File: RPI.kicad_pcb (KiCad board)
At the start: 2 copper layers, 65 x 56 mm, 31 parts, among them J1 Conn_01x02_Male, J2 GPIO, J5 Conn_01x06, J6 Conn_01x04, J7 Conn_01x03, J8 Conn_01x02, J9 Conn_01x02, Q1 IRF9540N, Q2 IRF9540N, Q3 BC856BDW1, SW1 SW_SPDT, SW2 SW_SPDT, U1 LM1085-ADJ

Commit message: Official completion (Maybe add Gerald in)
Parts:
- added G***: LOGO, LOGO, F.Cu at (124.0, 96.2)
- added ROBOTS101: LOGO, LOGO, F.Cu at (115.4, 59.9)
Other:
- board text added: "Motor LED"
- board text added: "Power Jumper"
- board text added: "Rasp Pi LED"
- board text added: "Remove jumper if powering board from the Raspberry Pi Keep jumper if powering board from the battery"
- board text removed: "R-Pi Batt Power Jumper"

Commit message: Student Version
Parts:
- removed C1: 10u, Capacitor_THT:CP_Radial_D5.0mm_P2.50mm
- removed C2: 10nF, Capacitor_SMD:C_0805_2012Metric_Pad1.18x1.45mm_HandSolder
- removed C3: 10uF, Capacitor_SMD:C_0805_2012Metric_Pad1.18x1.45mm_HandSolder
- removed C_Tan1: 10u, Capacitor_Tantalum_SMD:CP_EIA-2012-12_Kemet-R_Pad1.30x1.05mm_HandSolder
- removed D1, D2: LED, Diode_SMD:D_0805_2012Metric_Pad1.15x1.40mm_HandSolder
- removed D3, D4: 1N52318, Diode_THT:D_DO-35_SOD27_P7.62mm_Horizontal
- removed G***, ROBOTS101: LOGO, LOGO
- removed Q1, Q2: IRF9540N, Package_TO_SOT_THT:TO-220-3_Vertical
- removed Q3: BC856BDW1, Package_TO_SOT_SMD:SOT-363_SC-70-6
- removed R1: 121, Resistor_SMD:R_0805_2012Metric_Pad1.20x1.40mm_HandSolder
- removed R2: 365, Resistor_SMD:R_0805_2012Metric_Pad1.20x1.40mm_HandSolder
- removed R3, R4: R, Resistor_SMD:R_0805_2012Metric_Pad1.20x1.40mm_HandSolder
- removed R5: 10k, Resistor_SMD:R_0805_2012Metric_Pad1.20x1.40mm_HandSolder
- removed R6: 47k, Resistor_SMD:R_0805_2012Metric_Pad1.20x1.40mm_HandSolder
- removed SW1, SW2: SW_SPDT, RPi_Hat:Switch_SPDT_Jaycar
- removed U1: LM1085-ADJ, RPi_Hat:LM1085-5.0
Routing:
- net VCC: track 105.4 -> 0.00 mm
- net +5V: track 83.8 -> 0.00 mm, vias 1 -> 0
- net /GPIO2/SDA1: track 64.5 -> 0.53 mm
- net /GPIO3/SCL1: track 60.1 -> 0.68 mm
- net /GPIO4/GPCLK: track 52.9 -> 0.00 mm
- net VDDA: track 52.8 -> 0.00 mm
- net Net-(Q1-Pad3): track 48.4 -> 0.00 mm
- net +BATT: track 46.7 -> 0.00 mm
- net VD: track 42.2 -> 0.00 mm, vias 1 -> 0
- net /GPIO9/MISO: track 33.3 -> 0.00 mm
- net Net-(Q2-Pad1): track 32.7 -> 0.00 mm
- net /GPIO27/GEN2: track 32.0 -> 0.00 mm
- net /GPIO17/GEN0: track 28.4 -> 0.00 mm
- net /GPIO18/GEN1: track 23.0 -> 0.00 mm
- net Net-(R1-Pad2): track 22.7 -> 0.00 mm
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- removed copper zone on B.Cu, net GND
- removed copper zone on F.Cu, net GND
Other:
- board text removed: "3.3V"
- board text removed: "5V"
- board text removed: "Battery Switch"
- board text removed: "Board Protection"
- board text removed: "GND"
- board text removed: "GPIO17"
- board text removed: "GPIO18"
- board text removed: "GPIO2"
- board text removed: "GPIO27"
- board text removed: "GPIO3"
- board text removed: "GPIO4"
- board text removed: "GPIO9"
- board text removed: "Motor Control"
- board text removed: "Motor LED"
- board text removed: "Motor Pow"
- board text removed: "Power Jumper"
- board text removed: "Rasp Pi LED"
- board text removed: "Rasp Pi Protection"
- board text removed: "Rasp Pi Switch"
- board text removed: "Remove jumper if powering board from the Raspberry Pi Keep jumper if powering board from the battery"
- board text removed: "Servo Motor"
- board text removed: "Ultrasonic Sensor"
- board text removed: "V Batt"
- board text removed: "Voltage Reg"

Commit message: Revert "Student Version"
This reverts commit 96f77fa7ec59c85fd2b51f56cc1ae2b80deb0d98.
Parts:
- added C1: 10u, Capacitor_THT:CP_Radial_D5.0mm_P2.50mm, F.Cu at (154.8, 65.5)
- added C2: 10nF, Capacitor_SMD:C_0805_2012Metric_Pad1.18x1.45mm_HandSolder, F.Cu at (111.0, 67.0)
- added C3: 10uF, Capacitor_SMD:C_0805_2012Metric_Pad1.18x1.45mm_HandSolder, F.Cu at (111.0, 73.0)
- added C_Tan1: 10u, Capacitor_Tantalum_SMD:CP_EIA-2012-12_Kemet-R_Pad1.30x1.05mm_HandSolder, B.Cu at (141.9, 62.8)
- added D1: LED, Diode_SMD:D_0805_2012Metric_Pad1.15x1.40mm_HandSolder, F.Cu at (134.0, 73.0)
- added D2: LED, Diode_SMD:D_0805_2012Metric_Pad1.15x1.40mm_HandSolder, F.Cu at (134.0, 67.0)
- added D3: 1N52318, Diode_THT:D_DO-35_SOD27_P7.62mm_Horizontal, F.Cu at (123.8, 73.0)
- added D4: 1N52318, Diode_THT:D_DO-35_SOD27_P7.62mm_Horizontal, F.Cu at (123.8, 67.0)
- added G***: LOGO, LOGO, F.Cu at (124.0, 96.2)
- added Q1: IRF9540N, Package_TO_SOT_THT:TO-220-3_Vertical, F.Cu at (128.0, 89.1)
- added Q2: IRF9540N, Package_TO_SOT_THT:TO-220-3_Vertical, F.Cu at (128.0, 81.0)
- added Q3: BC856BDW1, Package_TO_SOT_SMD:SOT-363_SC-70-6, B.Cu at (142.0, 57.0)
- added R1: 121, Resistor_SMD:R_0805_2012Metric_Pad1.20x1.40mm_HandSolder, B.Cu at (134.0, 56.2)
- added R2: 365, Resistor_SMD:R_0805_2012Metric_Pad1.20x1.40mm_HandSolder, B.Cu at (129.0, 56.2)
- added R3: R, Resistor_SMD:R_0805_2012Metric_Pad1.20x1.40mm_HandSolder, B.Cu at (123.7, 56.2)
- added R4: R, Resistor_SMD:R_0805_2012Metric_Pad1.20x1.40mm_HandSolder, B.Cu at (123.7, 62.0)
- added R5: 10k, Resistor_SMD:R_0805_2012Metric_Pad1.20x1.40mm_HandSolder, B.Cu at (129.0, 62.0)
- added R6: 47k, Resistor_SMD:R_0805_2012Metric_Pad1.20x1.40mm_HandSolder, B.Cu at (134.0, 62.2)
- added ROBOTS101: LOGO, LOGO, F.Cu at (115.4, 59.9)
- added SW1: SW_SPDT, RPi_Hat:Switch_SPDT_Jaycar, F.Cu at (153.5, 77.0)
- added SW2: SW_SPDT, RPi_Hat:Switch_SPDT_Jaycar, F.Cu at (153.5, 89.0)
- added U1: LM1085-ADJ, RPi_Hat:LM1085-5.0, F.Cu at (152.0, 55.0)
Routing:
- net VCC: track 0.00 -> 105.4 mm
- net +5V: track 0.00 -> 83.8 mm, vias 0 -> 1
- net /GPIO2/SDA1: track 0.53 -> 64.5 mm
- net /GPIO3/SCL1: track 0.68 -> 60.1 mm
- net /GPIO4/GPCLK: track 0.00 -> 52.9 mm
- net VDDA: track 0.00 -> 52.8 mm
- net Net-(Q1-Pad3): track 0.00 -> 48.4 mm
- net +BATT: track 0.00 -> 46.7 mm
- net VD: track 0.00 -> 42.2 mm, vias 0 -> 1
- net /GPIO9/MISO: track 0.00 -> 33.3 mm
- net Net-(Q2-Pad1): track 0.00 -> 32.7 mm
- net /GPIO27/GEN2: track 0.00 -> 32.0 mm
- net /GPIO17/GEN0: track 0.00 -> 28.4 mm
- net /GPIO18/GEN1: track 0.00 -> 23.0 mm
- net Net-(R1-Pad2): track 0.00 -> 22.7 mm
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- added copper zone on B.Cu, net GND
- added copper zone on F.Cu, net GND
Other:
- board text added: "3.3V"
- board text added: "5V"
- board text added: "Battery Switch"
- board text added: "Board Protection"
- board text added: "GND"
- board text added: "GPIO17"
- board text added: "GPIO18"
- board text added: "GPIO2"
- board text added: "GPIO27"
- board text added: "GPIO3"
- board text added: "GPIO4"
- board text added: "GPIO9"
- board text added: "Motor Control"
- board text added: "Motor LED"
- board text added: "Motor Pow"
- board text added: "Power Jumper"
- board text added: "Rasp Pi LED"
- board text added: "Rasp Pi Protection"
- board text added: "Rasp Pi Switch"
- board text added: "Remove jumper if powering board from the Raspberry Pi Keep jumper if powering board from the battery"
- board text added: "Servo Motor"
- board text added: "Ultrasonic Sensor"
- board text added: "V Batt"
- board text added: "Voltage Reg"

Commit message: Added Fuse
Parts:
- added F1: MCCQ-122, RPi_Hat:MCCQ122, F.Cu at (124.3, 79.3)
- added G***: LOGO, LOGO, F.Cu at (153.8, 61.6)
- C2: renamed from C_Tan1; value 10u -> 100u
- moved Q1 6.08 mm to (134.1, 89.1)
- moved Q2 6.08 mm to (134.1, 81.0)
- renumbered C2 to C3, C3 to C4
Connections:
- Q1 pad 2: Net-(J1-Pad2) -> Net-(F1-Pad3)
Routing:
- net Net-(F1-Pad3): track 0.00 -> 20.1 mm
- net Net-(Q1-Pad3): track 48.4 -> 41.9 mm
- net VCC: track 105.4 -> 102.8 mm
- net VDDA: track 52.8 -> 50.3 mm
- net VD: track 42.2 -> 39.7 mm
- net Net-(J1-Pad2): track 19.7 -> 17.7 mm
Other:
- board text added: "F1"
- board text added: "Main Fuse"

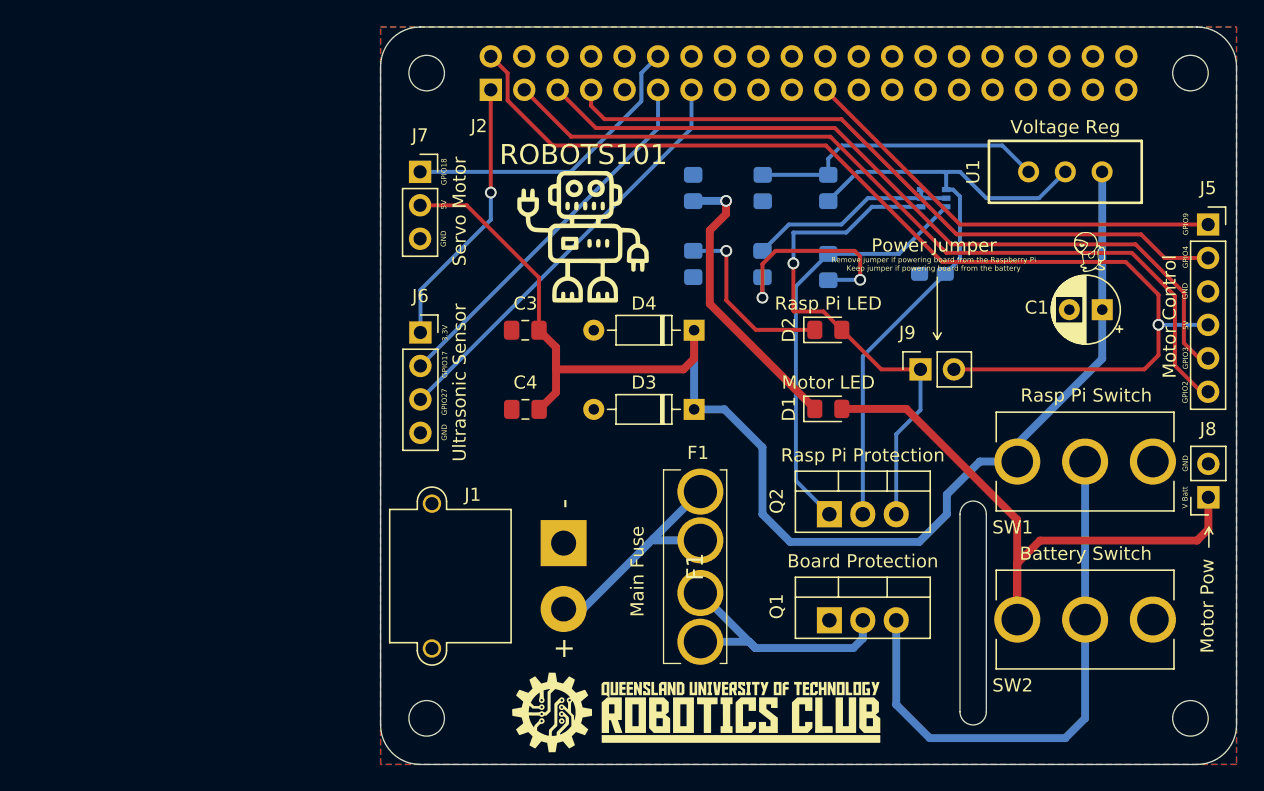
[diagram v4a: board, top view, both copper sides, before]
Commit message: V2 Overhaul with new circuits and GPIO routes
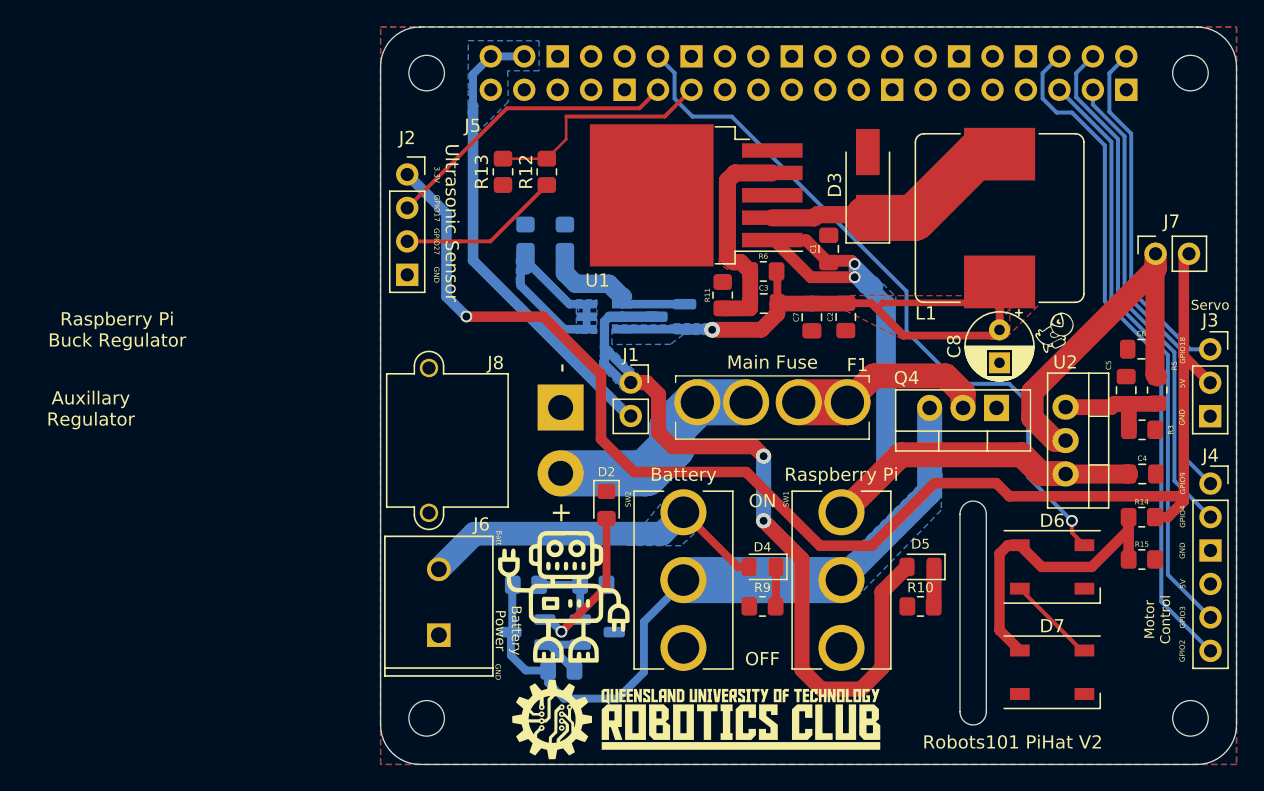
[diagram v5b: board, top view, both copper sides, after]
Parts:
- removed D1: LED, Diode_SMD:D_0805_2012Metric_Pad1.15x1.40mm_HandSolder
- removed the J5 at (162.8, 59.0)
- removed J9: Conn_01x02, Connector_PinSocket_2.54mm:PinSocket_1x02_P2.54mm_Vertical
- added C5: 10u, Capacitor_SMD:C_0805_2012Metric_Pad1.18x1.45mm_HandSolder, F.Cu at (156.6, 71.6)
- added C6: 22u T, Capacitor_SMD:C_0805_2012Metric_Pad1.18x1.45mm_HandSolder, F.Cu at (157.8, 68.5)
- added C7: C, Capacitor_SMD:C_0805_2012Metric_Pad1.18x1.45mm_HandSolder, F.Cu at (132.8, 66.0)
- added C8: C, Capacitor_THT:CP_Radial_D5.0mm_P2.50mm, F.Cu at (147.0, 67.0)
- added D5: LED, Diode_SMD:D_0805_2012Metric_Pad1.15x1.40mm_HandSolder, F.Cu at (141.0, 85.0)
- added D6: WS2812B, LED_SMD:LED_WS2812B_PLCC4_5.0x5.0mm_P3.2mm, F.Cu at (151.0, 85.0)
- added D7: WS2812B, LED_SMD:LED_WS2812B_PLCC4_5.0x5.0mm_P3.2mm, F.Cu at (151.0, 93.0)
- added J2: Conn_01x04, Connector_PinSocket_2.54mm:PinSocket_1x04_P2.54mm_Vertical, F.Cu at (102.0, 55.2)
- added J3: Conn_01x03, Connector_PinSocket_2.54mm:PinSocket_1x03_P2.54mm_Vertical, F.Cu at (163.0, 68.5)
- added J4: Conn_01x06, Connector_PinSocket_2.54mm:PinSocket_1x06_P2.54mm_Vertical, F.Cu at (163.0, 78.7)
- added L1: 48u, Inductor_SMD:L_Bourns_SRR1260, F.Cu at (147.0, 58.5)
- added Q4: IRF9540N, Package_TO_SOT_THT:TO-220-3_Vertical, F.Cu at (146.8, 72.9)
- added R10: R, Resistor_SMD:R_0805_2012Metric_Pad1.20x1.40mm_HandSolder, F.Cu at (141.0, 88.0)
- added R11: R, Resistor_SMD:R_0805_2012Metric_Pad1.20x1.40mm_HandSolder, F.Cu at (126.0, 64.4)
- added R12: 330, Resistor_SMD:R_0805_2012Metric_Pad1.20x1.40mm_HandSolder, F.Cu at (112.6, 55.0)
- added R13: 470, Resistor_SMD:R_0805_2012Metric_Pad1.20x1.40mm_HandSolder, F.Cu at (109.3, 55.0)
- added R14: R, Resistor_SMD:R_0805_2012Metric_Pad1.20x1.40mm_HandSolder, F.Cu at (157.8, 81.2)
- added R15: R, Resistor_SMD:R_0805_2012Metric_Pad1.20x1.40mm_HandSolder, F.Cu at (157.8, 84.4)
- added R7: 182K, Resistor_SMD:R_0805_2012Metric_Pad1.20x1.40mm_HandSolder, B.Cu at (111.0, 86.4)
- added R8: 100K, Resistor_SMD:R_0805_2012Metric_Pad1.20x1.40mm_HandSolder, B.Cu at (116.2, 86.4)
- added R9: R, Resistor_SMD:R_0805_2012Metric_Pad1.20x1.40mm_HandSolder, F.Cu at (129.0, 88.0)
- added U2: LM1085-5.0, Package_TO_SOT_THT:TO-220-3_Vertical, F.Cu at (152.0, 72.9)
- added U3: AZ431AN-ATRE1, Package_TO_SOT_SMD:SOT-23-3, B.Cu at (116.5, 90.0)
- C1: value 10u -> 100u; footprint Capacitor_THT:CP_Radial_D5.0mm_P2.50mm -> Capacitor_SMD:C_0805_2012Metric_Pad1.18x1.45mm_HandSolder
- C2: value 100u -> 220u; footprint Capacitor_Tantalum_SMD:CP_EIA-2012-12_Kemet-R_Pad1.30x1.05mm_HandSolder -> Capacitor_SMD:C_0805_2012Metric_Pad1.18x1.45mm_HandSolder; moved to F.Cu
- C3: value 10nF -> C
- C4: value 10uF -> 10u C
- D3: value 1N52318 -> SK34A; footprint Diode_THT:D_DO-35_SOD27_P7.62mm_Horizontal -> Diode_SMD:D_SMA_Handsoldering
- D4: value 1N52318 -> LED; footprint Diode_THT:D_DO-35_SOD27_P7.62mm_Horizontal -> Diode_SMD:D_0805_2012Metric_Pad1.15x1.40mm_HandSolder
- J1: value Conn_01x02_Male -> Conn_01x02; footprint Connector_AMASS:AMASS_XT30PW-M_1x02_P2.50mm_Horizontal -> Connector_PinSocket_2.54mm:PinSocket_1x02_P2.54mm_Vertical
- J6: value Conn_01x04 -> Conn_01x02; footprint Connector_PinSocket_2.54mm:PinSocket_1x04_P2.54mm_Vertical -> RPi_Hat:TE_282836-2
- J7: value Conn_01x03 -> Conn_01x02; footprint Connector_PinSocket_2.54mm:PinSocket_1x03_P2.54mm_Vertical -> Connector_PinSocket_2.54mm:PinSocket_1x02_P2.54mm_Vertical
- J8: value Conn_01x02 -> Conn_01x02_Male; footprint Connector_PinSocket_2.54mm:PinSocket_1x02_P2.54mm_Vertical -> Connector_AMASS:AMASS_XT30PW-M_1x02_P2.50mm_Horizontal
- Q1: value IRF9540N -> DMMT5401-7-F; footprint Package_TO_SOT_THT:TO-220-3_Vertical -> Package_TO_SOT_SMD:SOT-23-6_Handsoldering; moved to B.Cu
- Q2: value IRF9540N -> DGM2305UX; footprint Package_TO_SOT_THT:TO-220-3_Vertical -> Package_TO_SOT_SMD:SOT-23; moved to B.Cu
- Q3: value BC856BDW1 -> SS8050; footprint Package_TO_SOT_SMD:SOT-363_SC-70-6 -> Package_TO_SOT_SMD:SOT-23-3
- R1: value 121 -> 10k
- R2: value 365 -> 47k
- R3: value R -> 5k; moved to F.Cu
- R4: value R -> 2K
- R5: value 10k -> 121; moved to F.Cu
- R6: value 47k -> R; moved to F.Cu
- U1: value LM1085-ADJ -> LM2596S-5; footprint RPi_Hat:LM1085-5.0 -> Package_TO_SOT_SMD:TO-263-5_TabPin3
- moved J7 56.2 mm to (158.9, 61.2), turned to 90 degrees
- moved J8 49.7 mm to (113.7, 72.9), turned to 90 degrees
- moved C4 47.1 mm to (157.8, 77.9), turned to 0 degrees
- moved Q3 45.1 mm to (111.2, 90.0)
- moved R3 38.7 mm to (157.8, 74.6), turned to 180 degrees
- moved R4 32.5 mm to (113.7, 92.9), turned to 180 degrees
- moved R5 31.5 mm to (159.0, 71.6), turned to 90 degrees
- moved SW2 30.6 mm to (123.0, 86.0), turned to -90 degrees
- moved Q1 28.7 mm to (117.0, 66.0)
- moved U1 28.1 mm to (124.0, 56.8), turned to 180 degrees
- moved ROBOTS101 27.4 mm to (113.9, 87.3)
- moved R1 23.3 mm to (111.0, 60.0)
- moved D3 21.5 mm to (137.0, 56.0), turned to 90 degrees
- moved D2 21.5 mm to (117.2, 80.3), turned to -90 degrees
- moved C1 21.3 mm to (134.0, 60.9), turned to 90 degrees
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- renumbered G*** to G, J2 to J5
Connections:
- C3 pad 1: VCC -> Net-(C3-Pad1)
- C3 pad 2: GND -> VDDA
- D2 pad 1: Net-(D2-Pad1) -> GND
- D2 pad 2: VD -> Net-(D2-Pad2)
- D3 pad 1: VCC -> Net-(D3-Pad1)
- D4 pad 1: VCC -> Net-(D4-Pad1)
- D4 pad 2: GND -> +BATT
- F1 pad 1: Net-(J1-Pad2) -> Net-(F1-Pad1)
- F1 pad 2: Net-(J1-Pad2) -> Net-(F1-Pad1)
- J1 pad 1: GND -> VD
- J1 pad 2: Net-(J1-Pad2) -> +5V
- J5 pad 4: /5v -> +5V
- J6 pad 1: +3V3 -> GND
- J6 pad 2: /GPIO17/GEN0 -> +BATT
- J7 pad 1: /GPIO18/GEN1 -> +5VD
- J7 pad 2: VCC -> Vdrive
- J8 pad 1: +BATT -> GND
- J8 pad 2: GND -> Net-(F1-Pad1)
- Q1 pad 1: GND -> Net-(Q1-Pad1)
- Q1 pad 2: Net-(F1-Pad3) -> Net-(Q1-Pad1)
- Q1 pad 3: Net-(Q1-Pad3) -> Net-(Q1-Pad1)
- Q2 pad 1: Net-(Q2-Pad1) -> Net-(Q1-Pad4)
- Q3 pad 1: VDDA -> Net-(D2-Pad2)
- Q3 pad 3: Net-(Q2-Pad1) -> -BATT
- R1 pad 1: VDDA -> Net-(Q1-Pad1)
- R1 pad 2: Net-(R1-Pad2) -> GND
- R2 pad 1: Net-(R1-Pad2) -> Net-(Q1-Pad4)
- R3 pad 2: Net-(D1-Pad1) -> Net-(C5-Pad1)
- R4 pad 1: Net-(D2-Pad1) -> Net-(Q3-Pad2)
- R4 pad 2: GND -> -BATT
- R5 pad 1: Net-(Q3-Pad2) -> Net-(C5-Pad1)
- R5 pad 2: GND -> +5VD
- R6 pad 1: Net-(Q2-Pad1) -> Net-(C3-Pad1)
- R6 pad 2: GND -> VDDA
- SW1 pad 2: Net-(Q1-Pad3) -> -BATT
- SW2 pad 2: Net-(Q1-Pad3) -> -BATT
- U1 pad 1: Net-(R1-Pad2) -> VCC
- U1 pad 2: VDDA -> Net-(D3-Pad1)
- U1 pad 3: VCC -> GND
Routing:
- net Vdrive: track 0.00 -> 105.9 mm, vias 0 -> 1
- net /GPIO2/SDA1: track 64.5 -> 0.00 mm
- net /GPIO3/SCL1: track 60.1 -> 0.00 mm
- net -BATT: track 0.00 -> 54.4 mm
- net /GPIO4/GPCLK: track 52.9 -> 0.00 mm
- net /GPIO16: track 0.00 -> 51.6 mm
- net +5V: track 83.8 -> 35.5 mm, vias 1 -> 0
- net /GPIO19: track 0.00 -> 45.4 mm
- net Net-(Q1-Pad3): track 41.9 -> 0.00 mm
- net /GPIO20: track 0.00 -> 39.7 mm
- net VCC: track 102.8 -> 65.0 mm, vias 0 -> 2
- net /GPIO26: track 0.00 -> 33.6 mm
- net /GPIO9/MISO: track 33.3 -> 0.00 mm
- net Net-(Q2-Pad1): track 32.3 -> 0.00 mm
- net /GPIO18/GEN1: track 23.0 -> 54.5 mm, vias 0 -> 1
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- added copper zone on B.Cu, net +5V
- added copper zone on B.Cu, net +BATT
- added copper zone on B.Cu, net -BATT
- added copper zone on F.Cu, net Net-(C3-Pad1)
- added copper zone on B.Cu, net Net-(Q1-Pad1)
- added copper zone on B.Cu, net Net-(Q1-Pad4)
- added copper zone on B.Cu, net VCC
- added copper zone on F.Cu, net VCC
- added copper zone on B.Cu, net VD
- added copper zone on B.Cu, net VDDA
- added copper zone on F.Cu, net VDDA
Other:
- board text added: "Auxillary Regulator"
- board text added: "Batt"
- board text added: "Battery"
- board text added: "Battery Power"
- board text added: "GPIO Pinouts: - Servo PWM - GPIO 21 - Ultrasonic Sensors: = Trigger - GPIO 17 = Echo - GPIO 27 - Neopixels - GPIO 18 - MDD3A Motor Controller = M1A - GPIO 16 = M1B - GPIO 19 = M2A - GPIO 20 = M2B - GPIO 21"
- board text added: "How to use board: - To power board from raspberry pi microUSB, remove J1 jumper to disconnect circuit from battery - LED D2 next to XT30 terminal J8 will light up when battery is low; save your data and disconnect power to prevent undervolting your Pi - When connecting components, always connect ground first before Vcc"
- board text added: "OFF"
- board text added: "ON"
- board text added: "Raspberry Pi"
- board text added: "Raspberry Pi Buck Regulator"
- board text added: "Robots101 PiHat V2"
- board text added: "Servo"
- board text removed: "Battery Switch"
- board text removed: "Board Protection"
- board text removed: "F1"
- board text removed: "Motor LED"
- board text removed: "Motor Pow"
- board text removed: "Power Jumper"
- board text removed: "Rasp Pi LED"
- board text removed: "Rasp Pi Protection"
- board text removed: "Rasp Pi Switch"
- board text removed: "Remove jumper if powering board from the Raspberry Pi Keep jumper if powering board from the battery"
- board text removed: "Servo Motor"
- board text removed: "V Batt"
- board text removed: "Voltage Reg"
